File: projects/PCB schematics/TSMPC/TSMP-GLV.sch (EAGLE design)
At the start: 2 parts, among them X1 5566-6, X2 5566-2

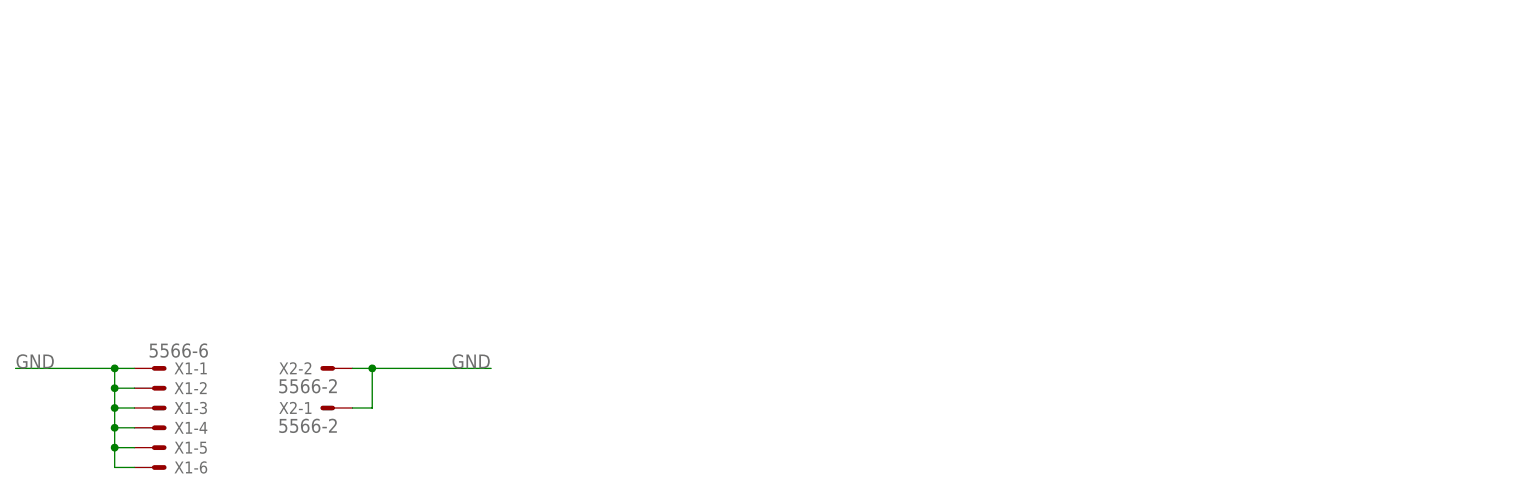
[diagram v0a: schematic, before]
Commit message: TSMPC - Board 3900milx3900mil redo.
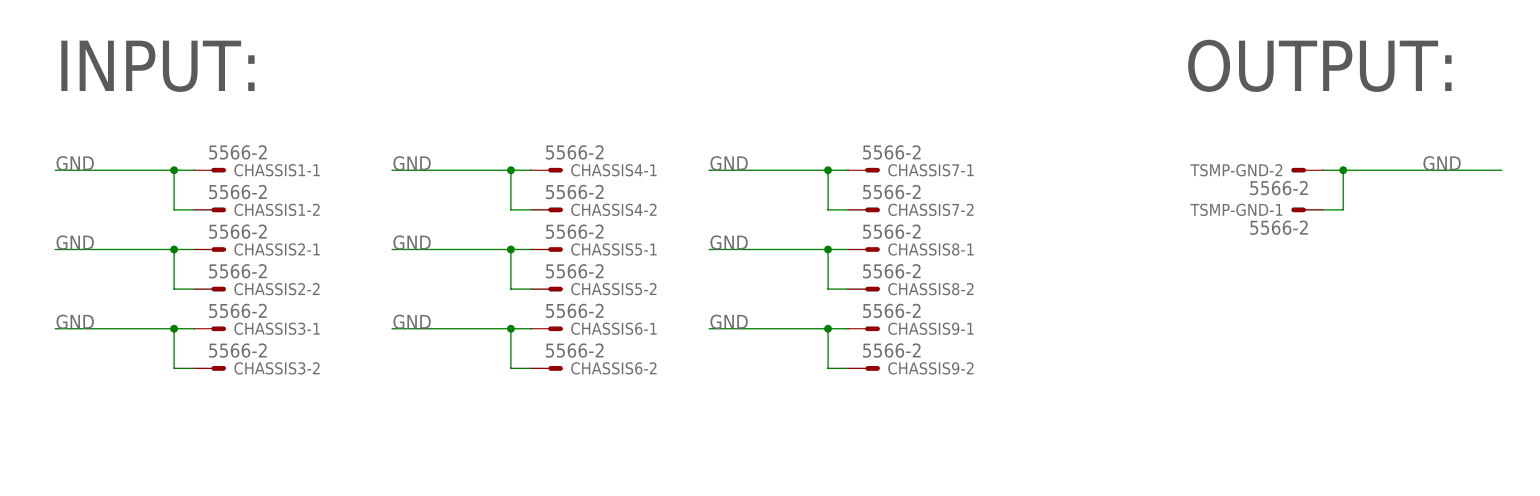
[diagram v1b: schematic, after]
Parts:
- removed X1: 5566-6, con-molex:5566-6
- removed X2: 5566-2, con-molex:5566-2
- added CHASSIS1, CHASSIS2, CHASSIS3, CHASSIS4, CHASSIS5, CHASSIS6, CHASSIS7, CHASSIS8, CHASSIS9, TSMP-GND: 5566-2, con-molex:5566-2
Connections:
- net GND: now also CHASSIS1-1.S, CHASSIS1-2.S, CHASSIS2-1.S, CHASSIS2-2.S, CHASSIS3-1.S, CHASSIS3-2.S, CHASSIS4-1.S, CHASSIS4-2.S, CHASSIS5-1.S, CHASSIS5-2.S, CHASSIS6-1.S, CHASSIS6-2.S, CHASSIS7-1.S, CHASSIS7-2.S, CHASSIS8-1.S, CHASSIS8-2.S, CHASSIS9-1.S, CHASSIS9-2.S, TSMP-GND-1.S, TSMP-GND-2.S; no longer X1-1.S, X1-2.S, X1-3.S, X1-4.S, X1-5.S, X1-6.S, X2-1.S, X2-2.S
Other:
- note added: "INPUT:"
- note added: "OUTPUT:"
